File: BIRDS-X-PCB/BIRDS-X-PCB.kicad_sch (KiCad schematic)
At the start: 0 parts

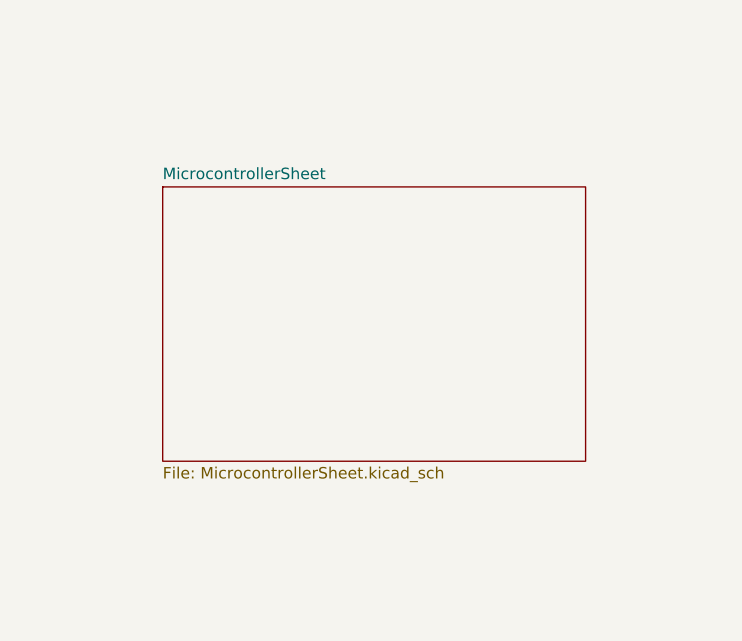
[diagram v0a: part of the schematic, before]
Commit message: Added microcontroller circuitry
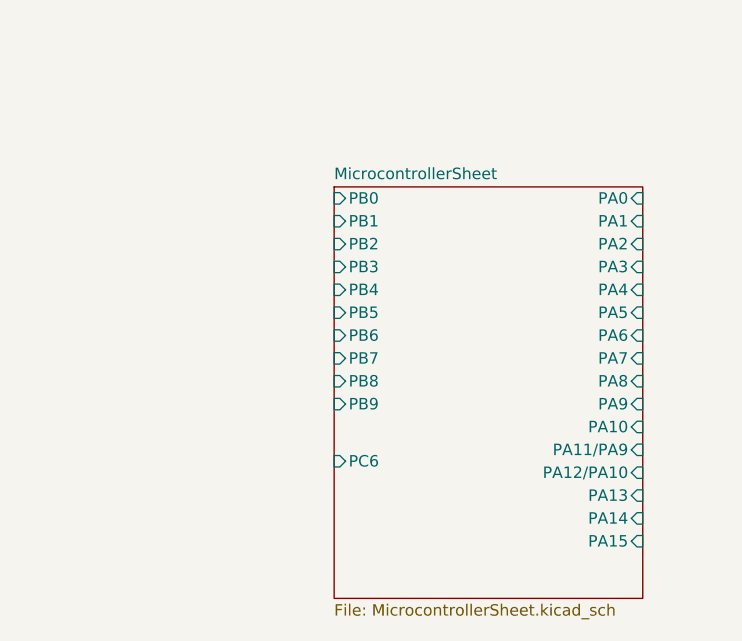
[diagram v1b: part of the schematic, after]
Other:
- sheet MicrocontrollerSheet ports: added PA0, PA1, PA10, PA11/PA9, PA12/PA10, PA13, PA14, PA15, PA2, PA3, PA4, PA5, PA6, PA7, PA8, PA9, PB0, PB1, PB2, PB3, PB4, PB5, PB6, PB7, PB8, PB9, PC6; removed none
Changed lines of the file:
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@@
     )
   )
-  (sheet (at 60.96 81.28) (size 46.99 30.48) (fields_autoplaced)
+  (sheet (at 80.01 81.28) (size 34.29 45.72) (fields_autoplaced)
     (stroke (width 0.1524) (type solid))
     (fill (color 0 0 0 0.0000))
-    (property "Sheetname" "MicrocontrollerSheet" (at 60.96 80.5684 0)
+    (property "Sheetname" "MicrocontrollerSheet" (at 80.01 80.5684 0)
       (effects (font (size 1.27 1.27)) (justify left bottom))
     )
-    (property "Sheetfile" "MicrocontrollerSheet.kicad_sch" (at 60.96 112.3446 0)
+    (property "Sheetfile" "MicrocontrollerSheet.kicad_sch" (at 80.01 127.5846 0)
       (effects (font (size 1.27 1.27)) (justify left top))
     )
+    (pin "PB7" input (at 80.01 100.33 180)
+      (effects (font (size 1.27 1.27)) (justify left))
+    )
+    (pin "PB8" input (at 80.01 102.87 180)
+      (effects (font (size 1.27 1.27)) (justify left))
+    )
+    (pin "PB9" input (at 80.01 105.41 180)
+      (effects (font (size 1.27 1.27)) (justify left))
+    )
+    (pin "PB0" input (at 80.01 82.55 180)
+      (effects (font (size 1.27 1.27)) (justify left))
+    )
+    (pin "PB1" input (at 80.01 85.09 180)
+      (effects (font (size 1.27 1.27)) (justify left))
+    )
+    (pin "PB2" input (at 80.01 87.63 180)
+      (effects (font (size 1.27 1.27)) (justify left))
+    )
+    (pin "PC6" input (at 80.01 111.76 180)
+      (effects (font (size 1.27 1.27)) (justify left))
+    )
+    (pin "PB6" input (at 80.01 97.79 180)
+      (effects (font (size 1.27 1.27)) (justify left))
+    )
+    (pin "PB3" input (at 80.01 90.17 180)
+      (effects (font (size 1.27 1.27)) (justify left))
+    )
+    (pin "PB4" input (at 80.01 92.71 180)
+      (effects (font (size 1.27 1.27)) (justify left))
+    )
+    (pin "PB5" input (at 80.01 95.25 180)
+      (effects (font (size 1.27 1.27)) (justify left))
+    )
+    (pin "PA7" input (at 114.3 100.33 0)
+      (effects (font (size 1.27 1.27)) (justify right))
+    )
+    (pin "PA8" input (at 114.3 102.87 0)
+      (effects (font (size 1.27 1.27)) (justify right))
+    )
+    (pin "PA10" input (at 114.3 107.95 0)
+      (effects (font (size 1.27 1.27)) (justify right))
+    )
+    (pin "PA12{slash}PA10" input (at 114.3 113.03 0)
+      (effects (font (size 1.27 1.27)) (justify right))
+    )
+    (pin "PA13" input (at 114.3 115.57 0)
+      (effects (font (size 1.27 1.27)) (justify right))
+    )
+    (pin "PA14" input (at 114.3 118.11 0)
+      (effects (font (size 1.27 1.27)) (justify right))
+    )
+    (pin "PA9" input (at 114.3 105.41 0)
+      (effects (font (size 1.27 1.27)) (justify right))
+    )
+    (pin "PA15" input (at 114.3 120.65 0)
+      (effects (font (size 1.27 1.27)) (justify right))
+    )
+    (pin "PA3" input (at 114.3 90.17 0)
+      (effects (font (size 1.27 1.27)) (justify right))
+    )
+    (pin "PA4" input (at 114.3 92.71 0)
+      (effects (font (size 1.27 1.27)) (justify right))
+    )
+    (pin "PA5" input (at 114.3 95.25 0)
+      (effects (font (size 1.27 1.27)) (justify right))
+    )
+    (pin "PA6" input (at 114.3 97.79 0)
+      (effects (font (size 1.27 1.27)) (justify right))
+    )
+    (pin "PA2" input (at 114.3 87.63 0)
+      (effects (font (size 1.27 1.27)) (justify right))
+    )
+    (pin "PA0" input (at 114.3 82.55 0)
+      (effects (font (size 1.27 1.27)) (justify right))
+    )
+    (pin "PA1" input (at 114.3 85.09 0)
+      (effects (font (size 1.27 1.27)) (justify right))
+    )
+    (pin "PA11{slash}PA9" input (at 114.3 110.49 0)
+      (effects (font (size 1.27 1.27)) (justify right))
+    )
     (instances

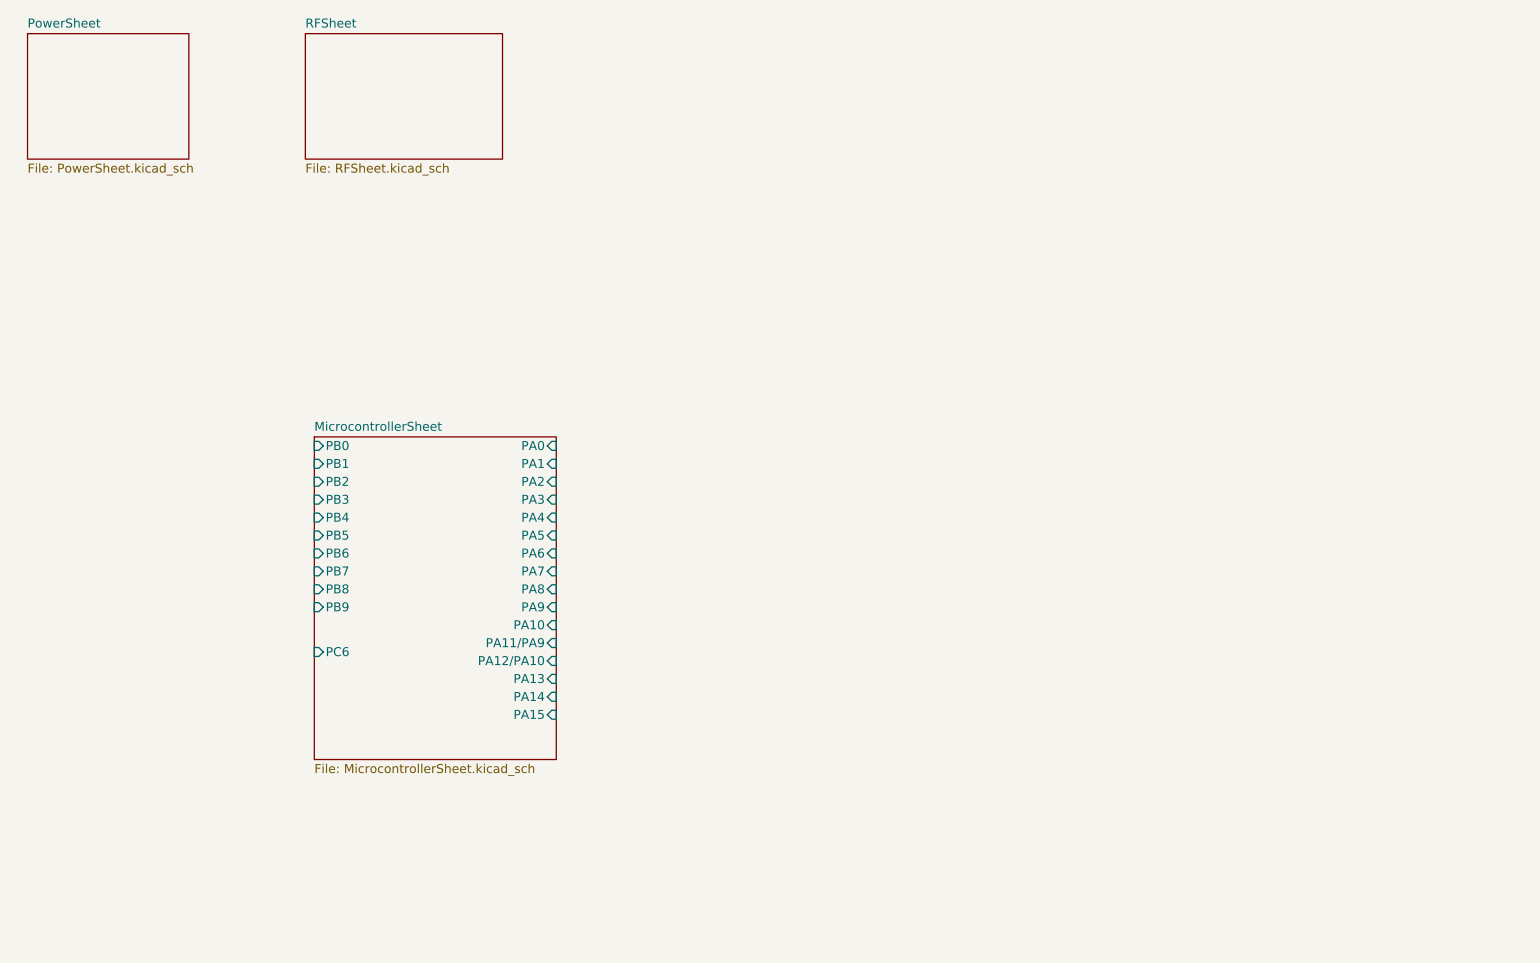
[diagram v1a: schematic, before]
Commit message: Migrate libraries, create LTC4361 symbol
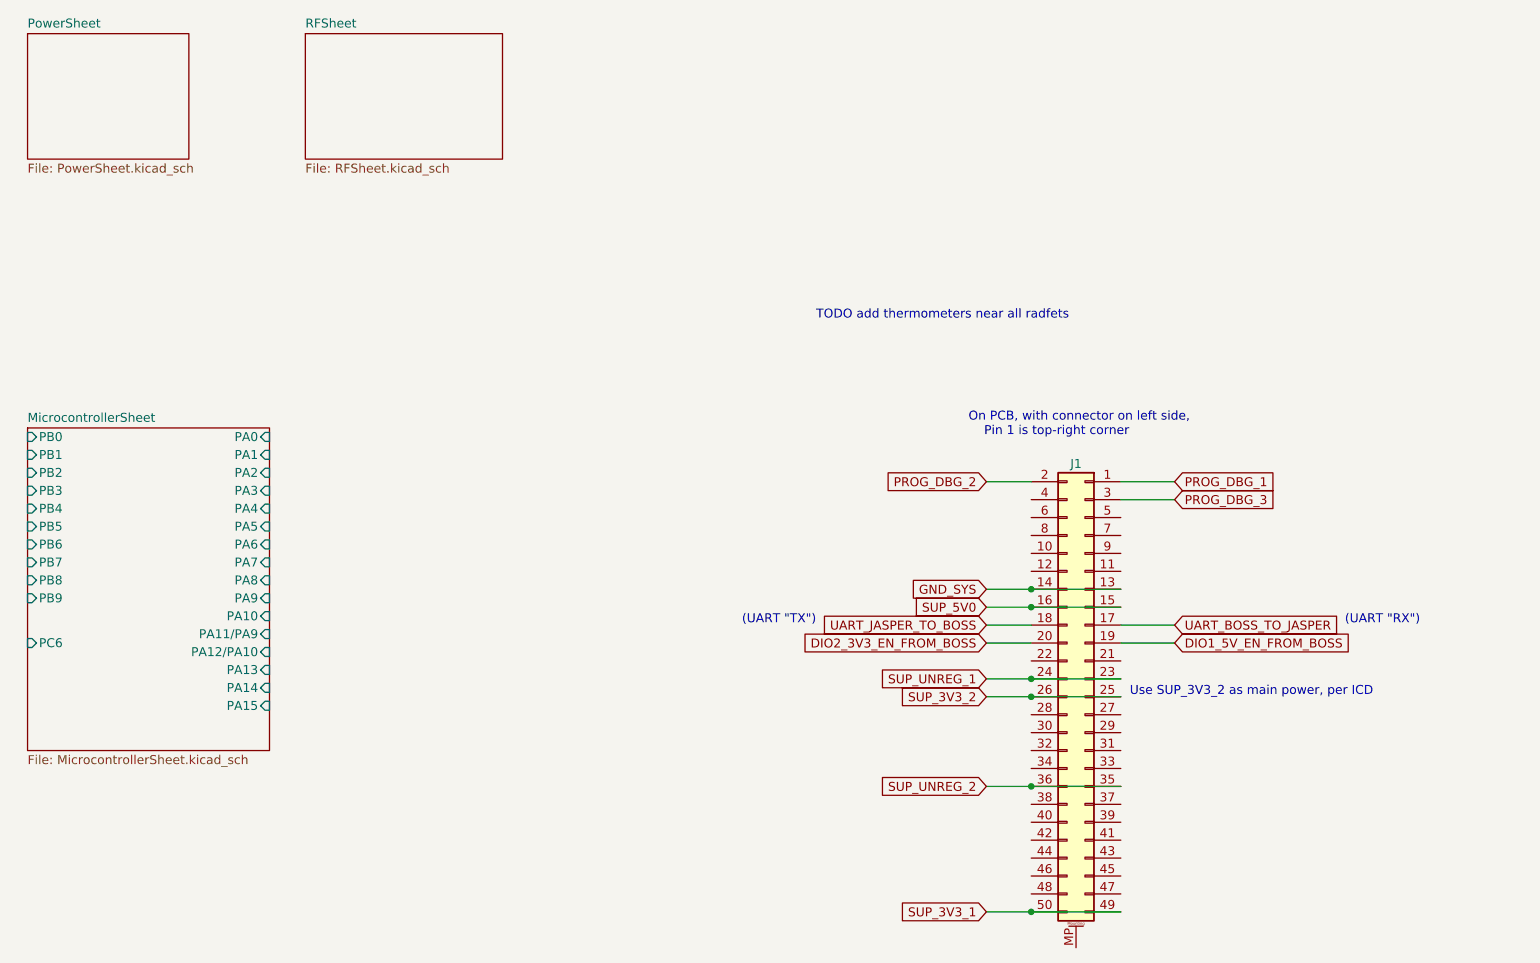
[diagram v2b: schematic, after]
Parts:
- added J1: Conn_02x25_Odd_Even_MountingPin, symbol Connector_Generic_MountingPin:Conn_02x25_Odd_Even_MountingPin
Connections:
- new net DIO1_5V_EN_FROM_BOSS: J1.19 (Pin_19)
- new net DIO2_3V3_EN_FROM_BOSS: J1.20 (Pin_20)
- new net GND_SYS: J1.13 (Pin_13), J1.14 (Pin_14)
- new net PROG_DBG_1: J1.1 (Pin_1)
- new net PROG_DBG_2: J1.2 (Pin_2)
- new net PROG_DBG_3: J1.3 (Pin_3)
- new net SUP_3V3_1: J1.49 (Pin_49), J1.50 (Pin_50)
- new net SUP_3V3_2: J1.25 (Pin_25), J1.26 (Pin_26)
- new net SUP_5V0: J1.15 (Pin_15), J1.16 (Pin_16)
- new net SUP_UNREG_1: J1.23 (Pin_23), J1.24 (Pin_24)
- new net SUP_UNREG_2: J1.35 (Pin_35), J1.36 (Pin_36)
- new net UART_BOSS_TO_JASPER: J1.17 (Pin_17)
- new net UART_JASPER_TO_BOSS: J1.18 (Pin_18)
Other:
- note added: "(UART "RX")"
- note added: "(UART "TX")"
- note added: "On PCB, with connector on left side, Pin 1 is top-right corner"
- note added: "TODO add thermometers near all radfets"
- note added: "Use SUP_3V3_2 as main power, per ICD"

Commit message: Add more components
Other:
- sheet RFSheet renamed Experiment
- sheet Experiment: file RFSheet.kicad_sch -> Experiment.kicad_sch
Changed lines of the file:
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@@
     (stroke (width 0.1524) (type solid))
     (fill (color 0 0 0 0.0000))
-    (property "Sheetname" "RFSheet" (at 78.74 23.4184 0)
+    (property "Sheetname" "Experiment" (at 78.74 23.4184 0)
       (effects (font (size 1.27 1.27)) (justify left bottom))
     )
-    (property "Sheetfile" "RFSheet.kicad_sch" (at 78.74 42.4946 0)
+    (property "Sheetfile" "Experiment.kicad_sch" (at 78.74 42.4946 0)
       (effects (font (size 1.27 1.27)) (justify left top))
     )

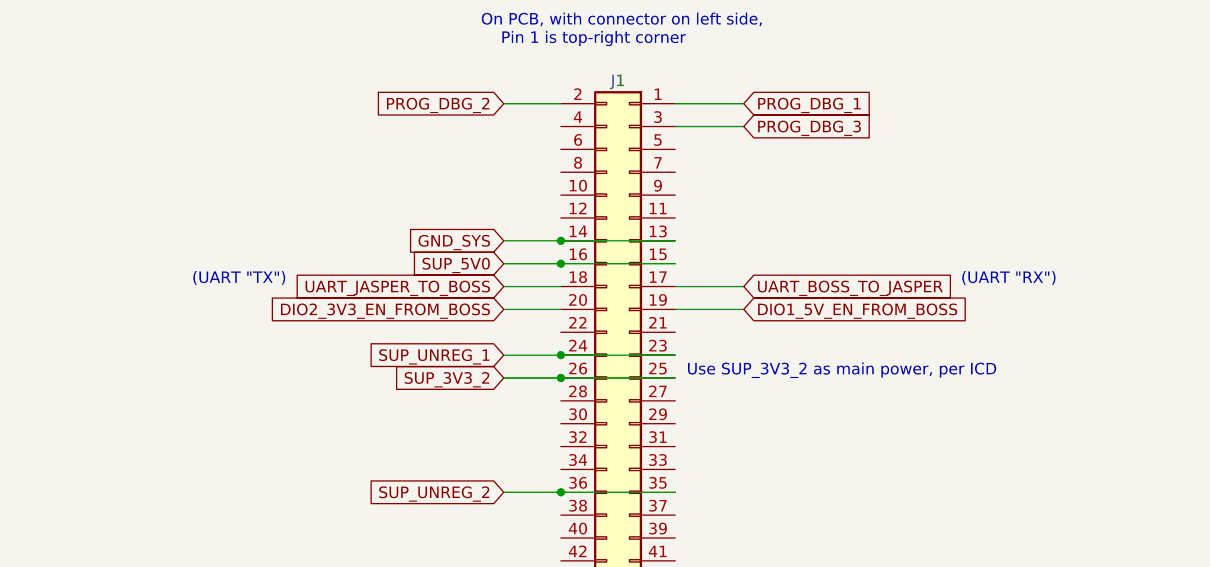
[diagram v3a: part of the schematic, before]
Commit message: Add flash, temperature sensor, etc.
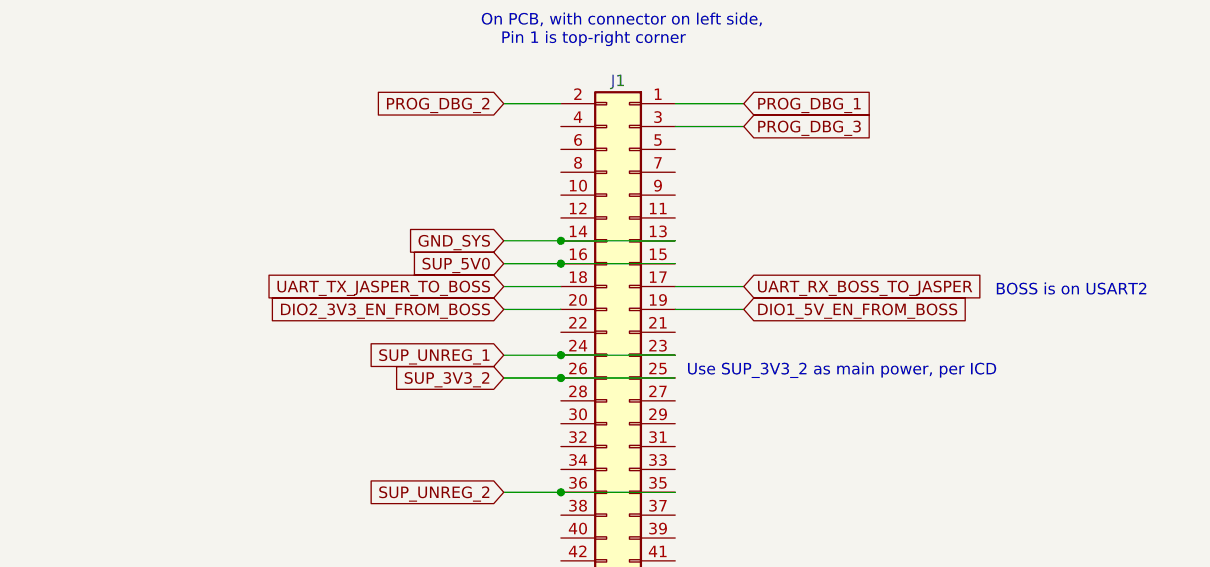
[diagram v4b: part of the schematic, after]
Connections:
- net UART_BOSS_TO_JASPER renamed UART_RX_BOSS_TO_JASPER
- net UART_JASPER_TO_BOSS renamed UART_TX_JASPER_TO_BOSS
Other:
- note added: "BOSS is on USART2"
- note removed: "(UART "RX")"
- note removed: "(UART "TX")"
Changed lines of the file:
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@@
     (stroke (width 0) (type default))
-  )
-  (text "(UART \"TX\")" (at 151.13 107.95 0)
-    (effects (font (size 1.27 1.27)) (justify right bottom))
   )
   (text "Use SUP_3V3_2 as main power, per ICD" (at 195.58 118.11 0)
@@
     (effects (font (size 1.27 1.27)) (justify left bottom))
   )
-  (text "(UART \"RX\")" (at 226.06 107.95 0)
+  (text "BOSS is on USART2" (at 229.87 109.22 0)
     (effects (font (size 1.27 1.27)) (justify left bottom))
   )
@@
     )
   )
-  (global_label "UART_BOSS_TO_JASPER" (shape input) (at 201.93 107.95 0) (fields_autoplaced)
+  (global_label "UART_RX_BOSS_TO_JASPER" (shape input) (at 201.93 107.95 0) (fields_autoplaced)
     (effects (font (size 1.27 1.27)) (justify left))
-    (property "Intersheetrefs" "${INTERSHEET_REFS}" (at 226.6676 107.95 0)
+    (property "Intersheetrefs" "${INTERSHEET_REFS}" (at 230.1147 107.95 0)
       (effects (font (size 1.27 1.27)) (justify left) hide)
     )
@@
     )
   )
-  (global_label "UART_JASPER_TO_BOSS" (shape input) (at 175.26 107.95 180) (fields_autoplaced)
+  (global_label "UART_TX_JASPER_TO_BOSS" (shape input) (at 175.26 107.95 180) (fields_autoplaced)
     (effects (font (size 1.27 1.27)) (justify right))
-    (property "Intersheetrefs" "${INTERSHEET_REFS}" (at 150.5224 107.95 0)
+    (property "Intersheetrefs" "${INTERSHEET_REFS}" (at 147.3777 107.95 0)
       (effects (font (size 1.27 1.27)) (justify right) hide)
     )
